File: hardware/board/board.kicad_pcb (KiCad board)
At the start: 2 copper layers, 40.1 x 49.3 mm, 52 parts, among them J1 Eurorack Power, J7 Tag-Connect SWD, J8 Big button, Q1 MMBT3904, U1 ATSAMD21G18A-AUT, U2 LM7805, U3 AP2112K-3.3, U4 LM4040LP-10, U5 TL072, U6 MCP6001-OT, U7 74AHCT1G125, U8 GD25Q16C

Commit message: Fix incorrect resistor values
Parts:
- CV_IN1: renamed from CV IN
- GATE_IN1: renamed from GATE IN
- GATE_OUT1: renamed from GATE OUT
- HONK_OUT1: renamed from HONK OUT
- R5: value 6.8k -> 100k
- R6: value 6.8k -> 200k
- R7: value 6.8k -> 33k
- renumbered J8 to Button1, RESET to RESET1, J7 to SWD1, USB to USB1
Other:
- board text added: "Winterbloom v2 3/5/2020 CC BY-SA 4.0 wntr.dev/honk"
- board text removed: "Winterbloom v1 2/26/2020 CC BY-SA 4.0 wntr.dev/honk"

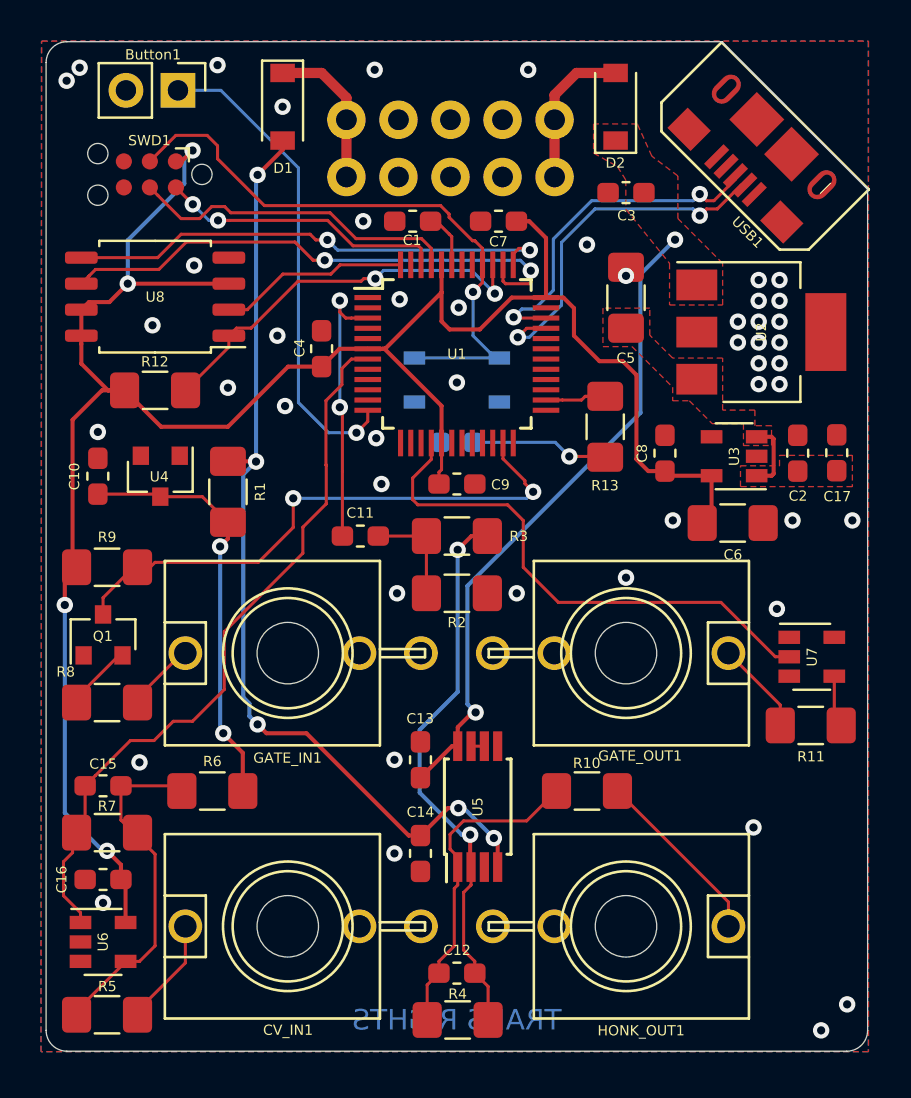
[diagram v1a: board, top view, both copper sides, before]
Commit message: Fix issues found in the first prototype
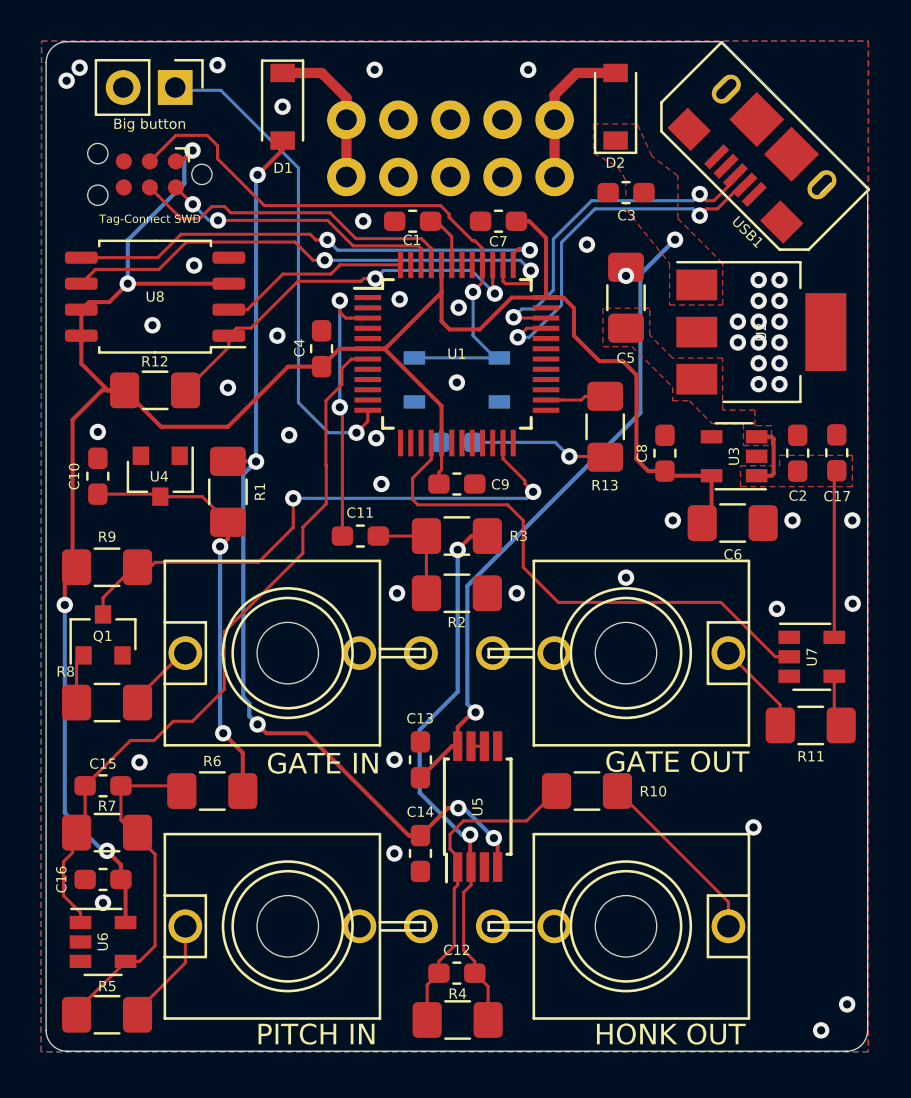
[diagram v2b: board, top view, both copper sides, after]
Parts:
- R6: value 200k -> 510k
- R7: value 33k -> 82k
- moved Button1 0.19 mm to (83.6, 101.2)
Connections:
- Q1 pad 1: GND -> Net-(Q1-Pad1)
- Q1 pad 2: Net-(Q1-Pad2) -> GND
- R8 pad 1: Net-(Q1-Pad2) -> Net-(Q1-Pad1)
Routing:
- net +5V: track 3.82 -> 12.0 mm
- net Net-(Q1-Pad2): track 3.43 -> 0.00 mm
- net Net-(Q1-Pad1): track 0.00 -> 2.44 mm
- net GND: track 0.00 -> 0.17 mm, vias 48 -> 49
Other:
- net class Default: clearance 0.2 -> 0.15
- rule trace_clearance: 0.2 -> 0.15
- rule trace_min: 0.15 -> 0.127
- board text added: "GATE IN"
- board text added: "GATE OUT"
- board text added: "HONK OUT"
- board text added: "PITCH IN"
- board text added: "Winterbloom v3 3/19/2020 CC BY-SA 4.0 wntr.dev/honk"
- board text removed: "Winterbloom v2 3/5/2020 CC BY-SA 4.0 wntr.dev/honk"

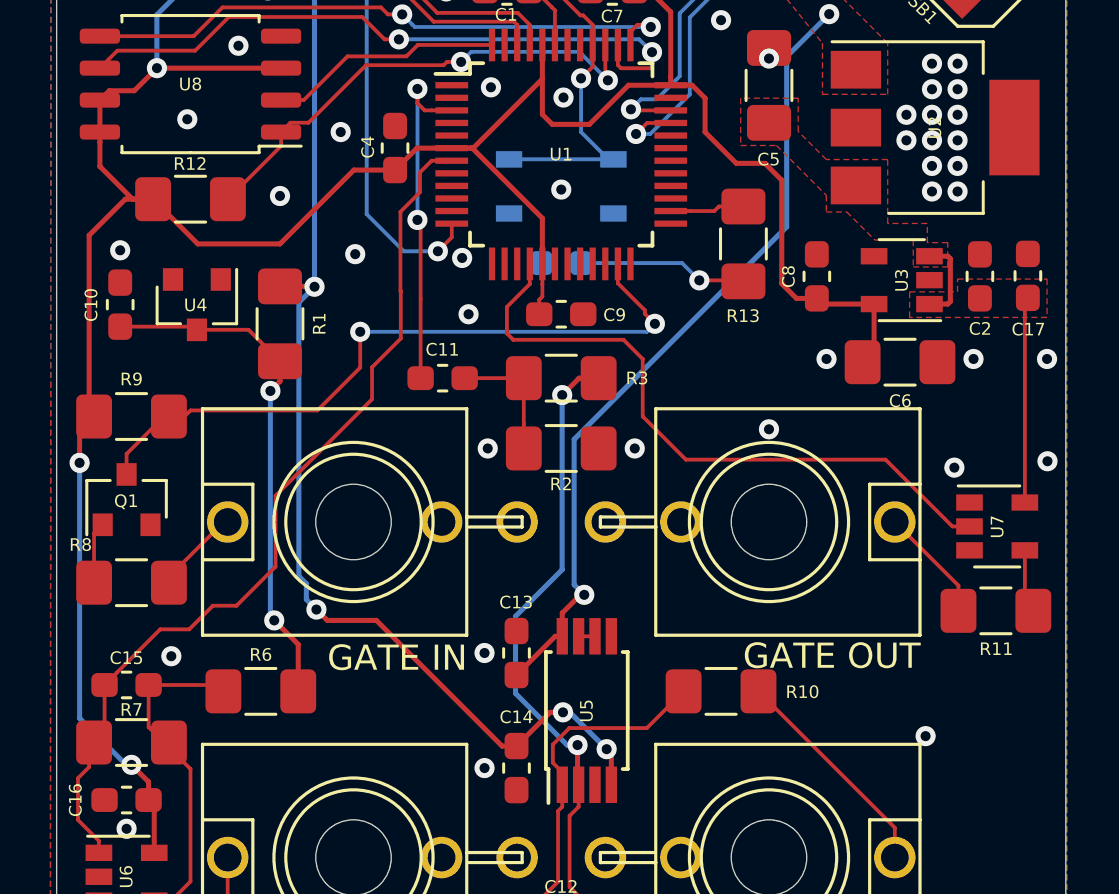
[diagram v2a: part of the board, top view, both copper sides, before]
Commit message: Fix pinout on zener diode
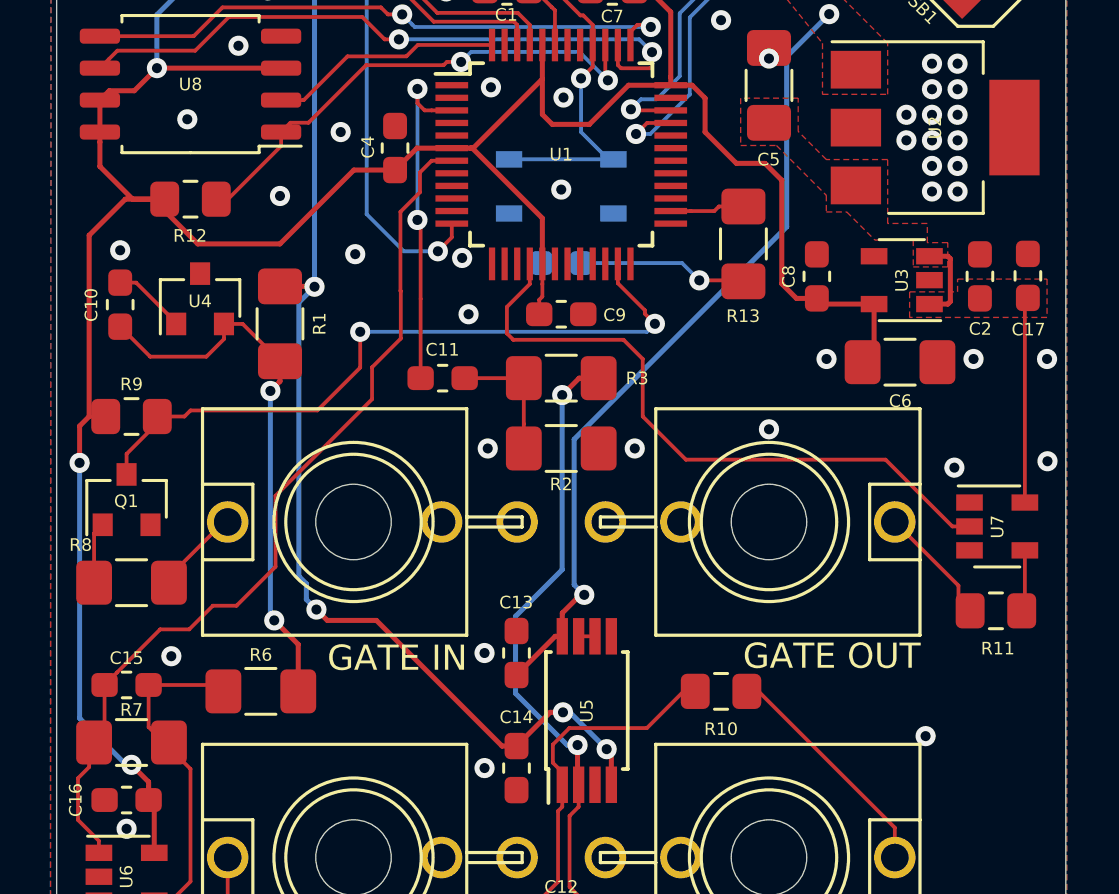
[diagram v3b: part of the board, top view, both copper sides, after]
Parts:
- R10, R11, R12, R9: footprint Resistor_SMD:R_1206_3216Metric_Pad1.42x1.75mm_HandSolder -> Resistor_SMD:R_0805_2012Metric_Pad1.15x1.40mm_HandSolder
- U4: value LM4040LP-10 -> LM4040DBZ-10
- moved U4 0.27 mm to (83.0, 119.9), turned to 90 degrees
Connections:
- U4 pad 1: (no net) -> GND
- U4 pad 2: GND -> VREF_-10
- U4 pad 3: VREF_-10 -> (no net)
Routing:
- net GND: track 0.17 -> 3.11 mm
- net VREF_-10: track 20.7 -> 22.1 mm
- net +3V3: track 108.4 -> 109.1 mm
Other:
- board text added: "Winterbloom v4 4/15/2020 CC BY-SA 4.0 wntr.dev/honk"
- board text removed: "Winterbloom v3 3/19/2020 CC BY-SA 4.0 wntr.dev/honk"

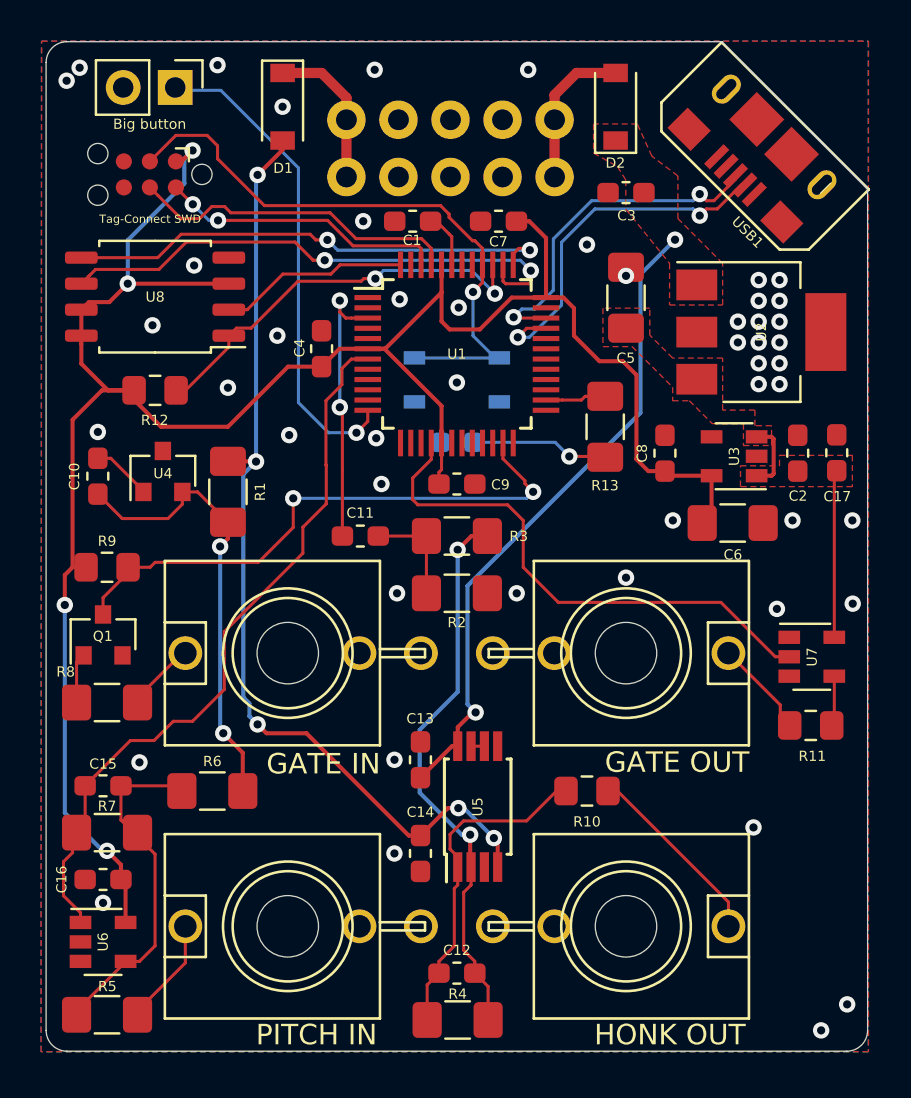
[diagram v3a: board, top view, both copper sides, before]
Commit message: Board revision v5
- Switch to 8mb flash
- Switch all resistors to 0603
- Change CV input to -5 to +5
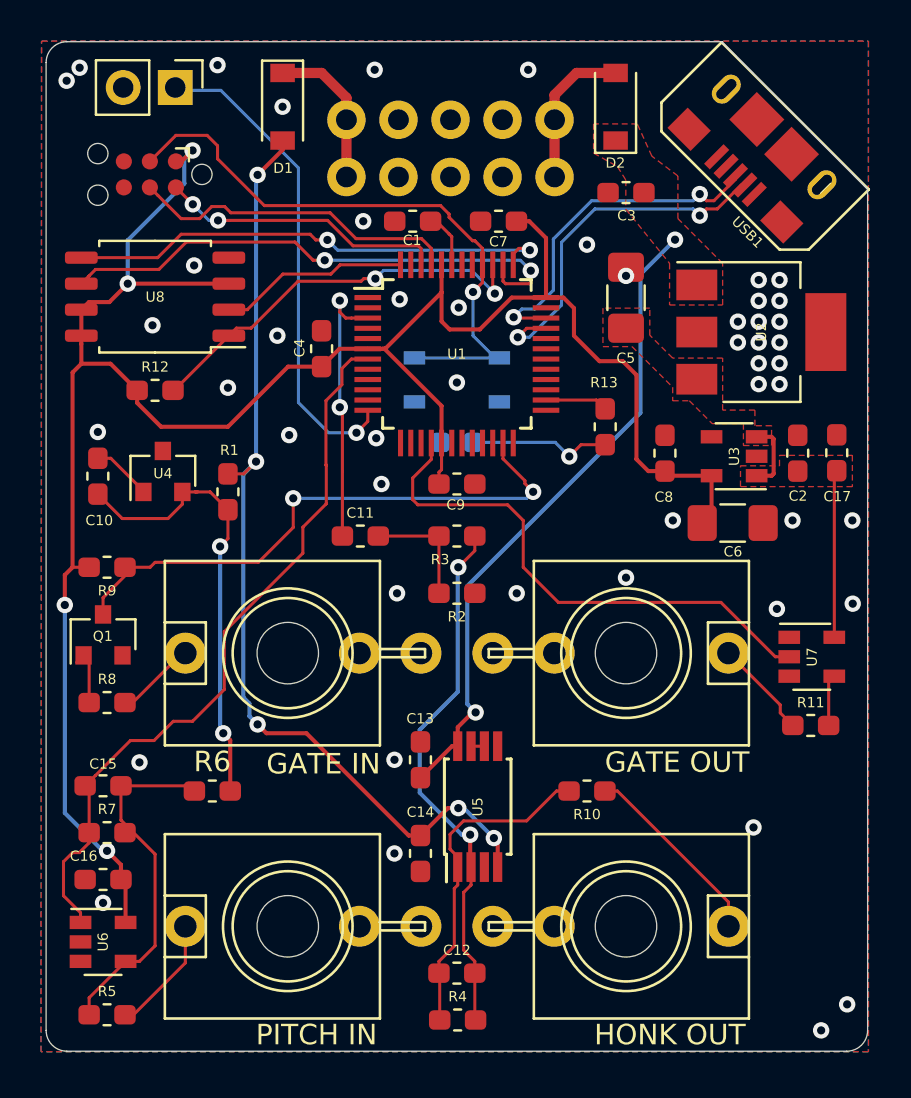
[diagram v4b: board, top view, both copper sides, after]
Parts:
- added G***: LOGO, board:winterbloom, B.Cu at (95.9, 121.1)
- added G***: LOGO, board:cc_by_sa, B.Cu at (97.4, 137.6)
- R1, R2, R3, R4, R5, R8: footprint Resistor_SMD:R_1206_3216Metric_Pad1.42x1.75mm_HandSolder -> Resistor_SMD:R_0603_1608Metric_Pad1.05x0.95mm_HandSolder
- R10, R11, R12, R9: footprint Resistor_SMD:R_0805_2012Metric_Pad1.15x1.40mm_HandSolder -> Resistor_SMD:R_0603_1608Metric_Pad1.05x0.95mm_HandSolder
- R13: value 2.2k -> 1k; footprint Resistor_SMD:R_1206_3216Metric_Pad1.42x1.75mm_HandSolder -> Resistor_SMD:R_0603_1608Metric_Pad1.05x0.95mm_HandSolder
- R6: value 510k -> 200k; footprint Resistor_SMD:R_1206_3216Metric_Pad1.42x1.75mm_HandSolder -> Resistor_SMD:R_0603_1608Metric_Pad1.05x0.95mm_HandSolder
- R7: value 82k -> 33k; footprint Resistor_SMD:R_1206_3216Metric_Pad1.42x1.75mm_HandSolder -> Resistor_SMD:R_0603_1608Metric_Pad1.05x0.95mm_HandSolder
- U8: value GD25Q16C -> GD25Q64C
- moved REF** 29.9 mm to (81.5, 144.9)
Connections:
- U1 pad 19: Net-(U1-Pad19) -> GND
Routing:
- net Net-(C12-Pad2): track 27.4 -> 26.4 mm
- net Net-(C11-Pad2): track 5.14 -> 5.76 mm
- net AUDIO_OUT: track 8.85 -> 9.46 mm
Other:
- board text added: "v5 10/7/2020 CC BY-SA 4.0 wntr.dev/honk"
- board text removed: "Winterbloom v4 4/15/2020 CC BY-SA 4.0 wntr.dev/honk"
